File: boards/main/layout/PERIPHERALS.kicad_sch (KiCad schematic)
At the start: 31 parts, among them Q1 AO3400A, SW1 DSHP04TJGER, SW2 GT-TC048B-H025-L1, SW3 GT-TC048B-H025-L1, SW5 GT-TC048B-H025-L1, U2 GT-USB-7010ASV

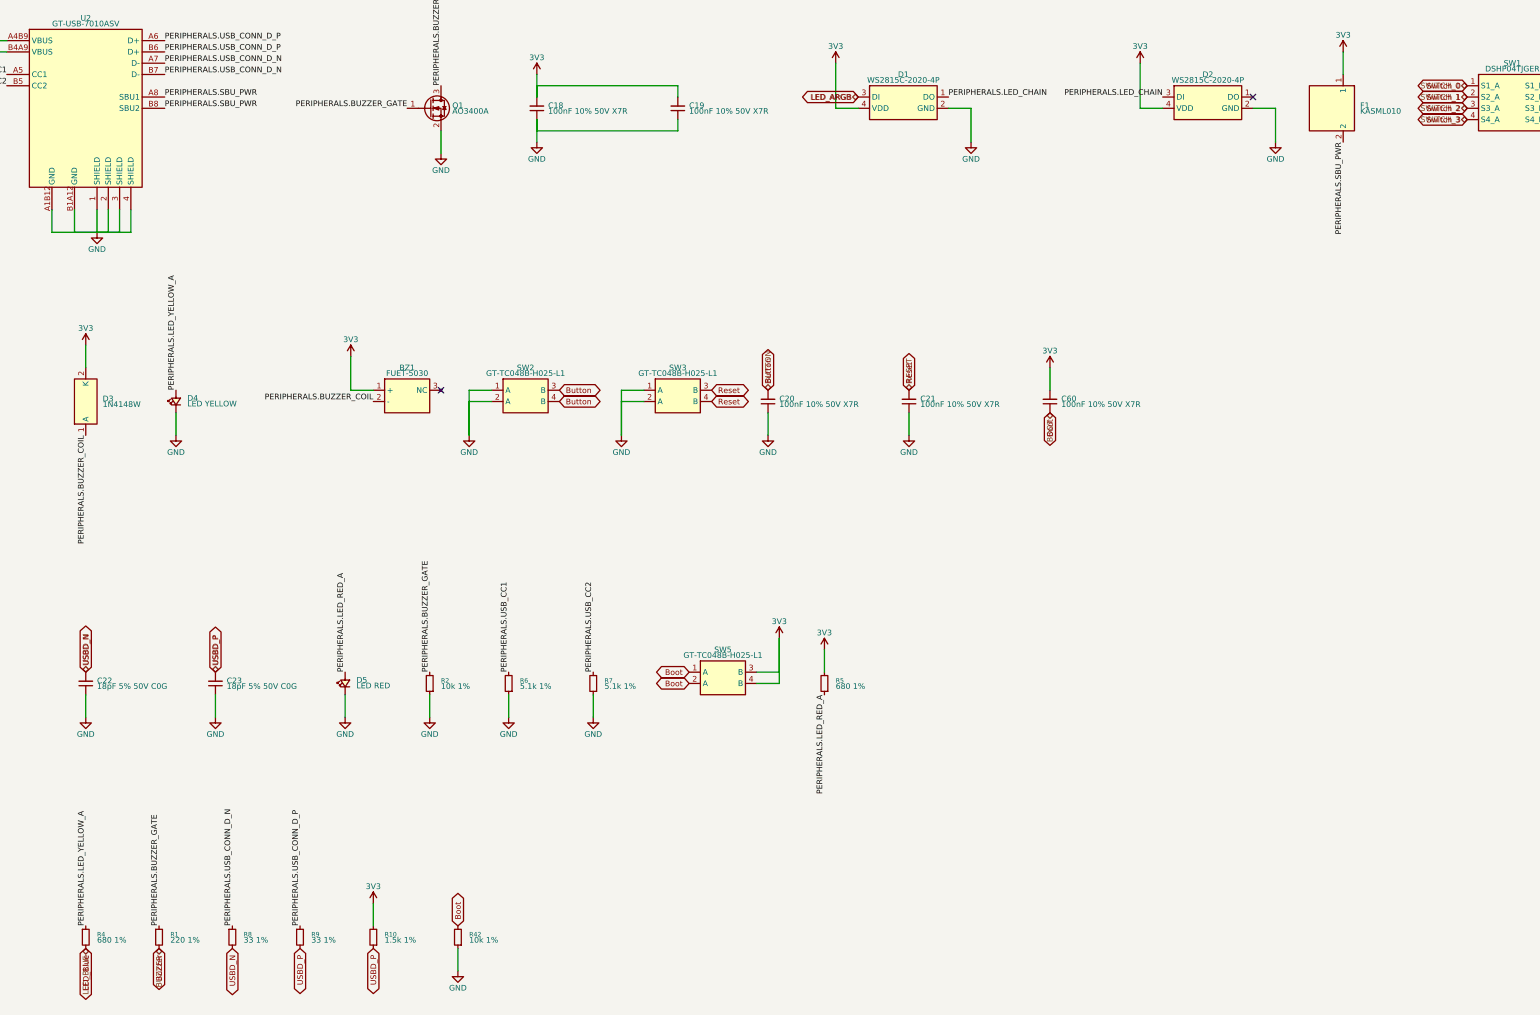
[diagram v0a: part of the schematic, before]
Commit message: 🏷️ Name the main board's module ports after their nets
A module's signal port now takes the name of the board net it carries (Fan_Enable, Wall_Sensor_0, Button), so its sheet pin and hierarchical label match the root's label: KiCad's ERC flagged each pair as similar_labels, names that differ only in case. The SPI buses and the Motor_*_Sense+/- nets, whose names are not identifiers, keep their port names. GND_BAT becomes a ground port of REGULATORS, so it reaches the root as a power symbol at the sheet pin instead of a dangling label. The netlist is unchanged: same nets, same names.
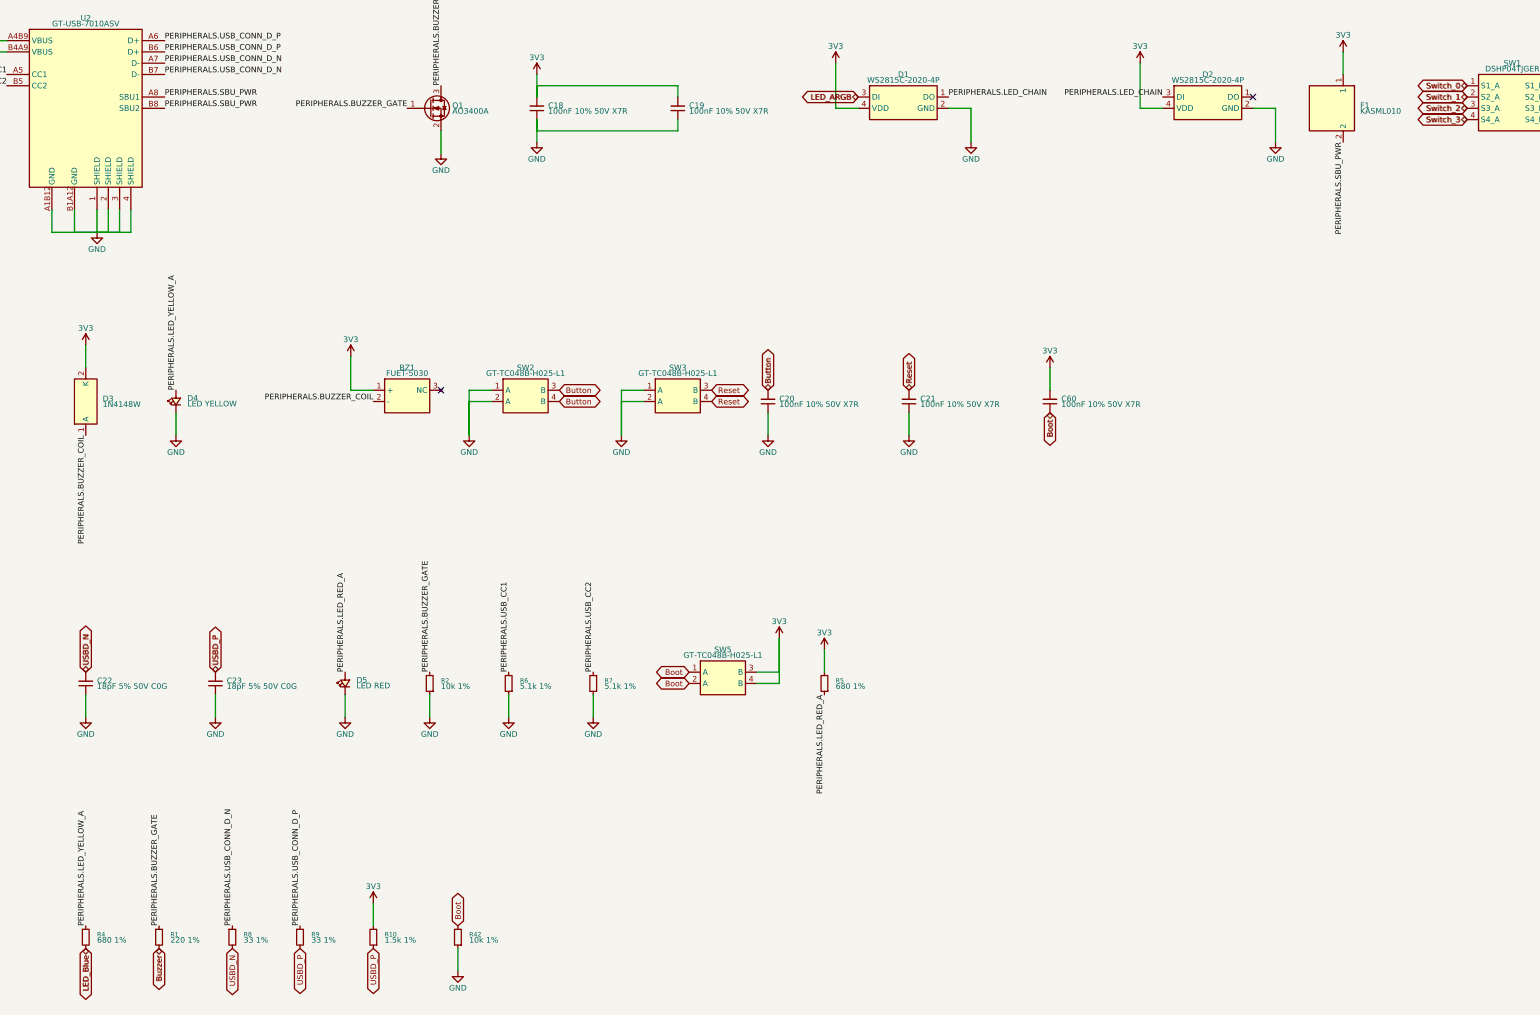
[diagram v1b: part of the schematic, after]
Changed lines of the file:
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@@
-		)
-	)
-	(hierarchical_label "SWITCH_0"
-		(shape bidirectional)
-		(at 358.14 53.34 180)
-		(effects
-			(font
-				(size 1.27 1.27)
-			)
-			(justify right)
 		)
 	)
@@
 		)
 	)
+	(hierarchical_label "Boot"
+		(shape bidirectional)
+		(at 264.16 127 270)
+		(effects
+			(font
+				(size 1.27 1.27)
+			)
+			(justify right)
+		)
+	)
+	(hierarchical_label "Switch_0"
+		(shape bidirectional)
+		(at 358.14 53.34 180)
+		(effects
+			(font
+				(size 1.27 1.27)
+			)
+			(justify right)
+		)
+	)
 	(hierarchical_label "LED_ARGB"
 		(shape bidirectional)
@@
 		)
 	)
-	(hierarchical_label "BOOT"
+	(hierarchical_label "LED_Blue"
 		(shape bidirectional)
-		(at 264.16 127 270)
+		(at 46.99 247.65 270)
 		(effects
 			(font
@@
 		)
 	)
-	(hierarchical_label "BUZZER"
+	(hierarchical_label "Switch_2"
 		(shape bidirectional)
-		(at 63.5 247.65 270)
+		(at 358.14 58.42 180)
 		(effects
 			(font
@@
 		)
 	)
-	(hierarchical_label "BUTTON"
+	(hierarchical_label "Switch_3"
 		(shape bidirectional)
-		(at 200.66 121.92 90)
-		(effects
-			(font
-				(size 1.27 1.27)
-			)
-			(justify left)
-		)
-	)
-	(hierarchical_label "SWITCH_1"
-		(shape bidirectional)
-		(at 358.14 55.88 180)
+		(at 358.14 60.96 180)
 		(effects
 			(font
@@
 		)
 	)
-	(hierarchical_label "SWITCH_3"
+	(hierarchical_label "Reset"
 		(shape bidirectional)
-		(at 358.14 60.96 180)
+		(at 232.41 121.92 90)
 		(effects
 			(font
 				(size 1.27 1.27)
 			)
-			(justify right)
+			(justify left)
 		)
 	)
@@
 		)
 	)
-	(hierarchical_label "SWITCH_2"
+	(hierarchical_label "Button"
 		(shape bidirectional)
-		(at 358.14 58.42 180)
+		(at 200.66 121.92 90)
+		(effects
+			(font
+				(size 1.27 1.27)
+			)
+			(justify left)
+		)
+	)
+	(hierarchical_label "Buzzer"
+		(shape bidirectional)
+		(at 63.5 247.65 270)
 		(effects
 			(font
@@
 		)
 	)
-	(hierarchical_label "RESET"
+	(hierarchical_label "Switch_1"
 		(shape bidirectional)
-		(at 232.41 121.92 90)
+		(at 358.14 55.88 180)
 		(effects
 			(font
-				(size 1.27 1.27)
-			)
-			(justify left)
-		)
-	)
-	(hierarchical_label "LED_BLUE"
-		(shape bidirectional)
-		(at 46.99 247.65 270)
-		(effects
-			(font

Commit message: 🎨 Place this revision's root, REGULATORS and SENSORS sheets; give the CJA1117B room for its pin names
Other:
- note added: "Addressable LEDs on VBAT"
- note added: "Bluetooth module supply on SBU: CC signature detector and switch"
- note added: "Buttons: user, reset, boot"
- note added: "Buzzer: low-side switch Q1, flyback D3"
- note added: "DIP switch"
- note added: "Indicator LEDs"
- note added: "Sheet ports"
- note added: "USB-C receptacle: VBUS sense, CC sink, ESD"
- title: (none) -> User interface and USB-C
- moved on the sheet: BZ1, C18, C19, C20, C21, C60, D1, D2, D3, D4, D5, F1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

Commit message: 🎨 Place this revision's PERIPHERALS sheet
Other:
- note added: "Addressable LEDs: WS2815C chain on 3V3"
- note added: "USB-C receptacle: CC sink, D+/D- series resistors, SBU supply fuse"
- note removed: "Addressable LEDs on VBAT"
- note removed: "Bluetooth module supply on SBU: CC signature detector and switch"
- note removed: "USB-C receptacle: VBUS sense, CC sink, ESD"
- moved on the sheet: BZ1, C18, C19, C20, C21, C22, C23, C60, D1, D2, D3, D4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
